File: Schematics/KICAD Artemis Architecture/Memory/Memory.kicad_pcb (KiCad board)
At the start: 4 copper layers, 100.1 x 45.8 mm, 11 parts, among them IC1 AT28C64B-15PU, IC2 AS7C164A-15PCN, IC3 AT28C64B-15PU, IC4 AS7C164A-15PCN, J1 Bus LB, J2 Bus UB, J3 Control, J4 Power, J5 Address, U1 74LS00

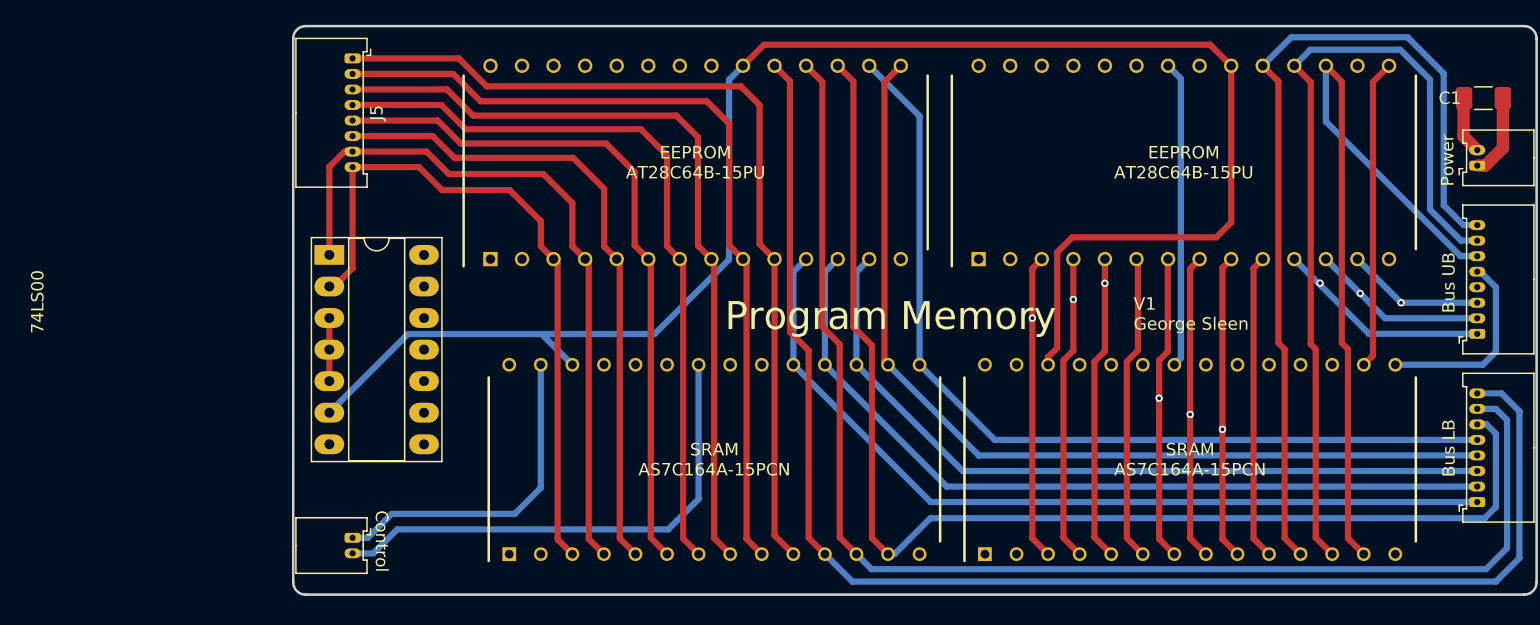
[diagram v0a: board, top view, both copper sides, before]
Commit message: Finished Program Memory PCB
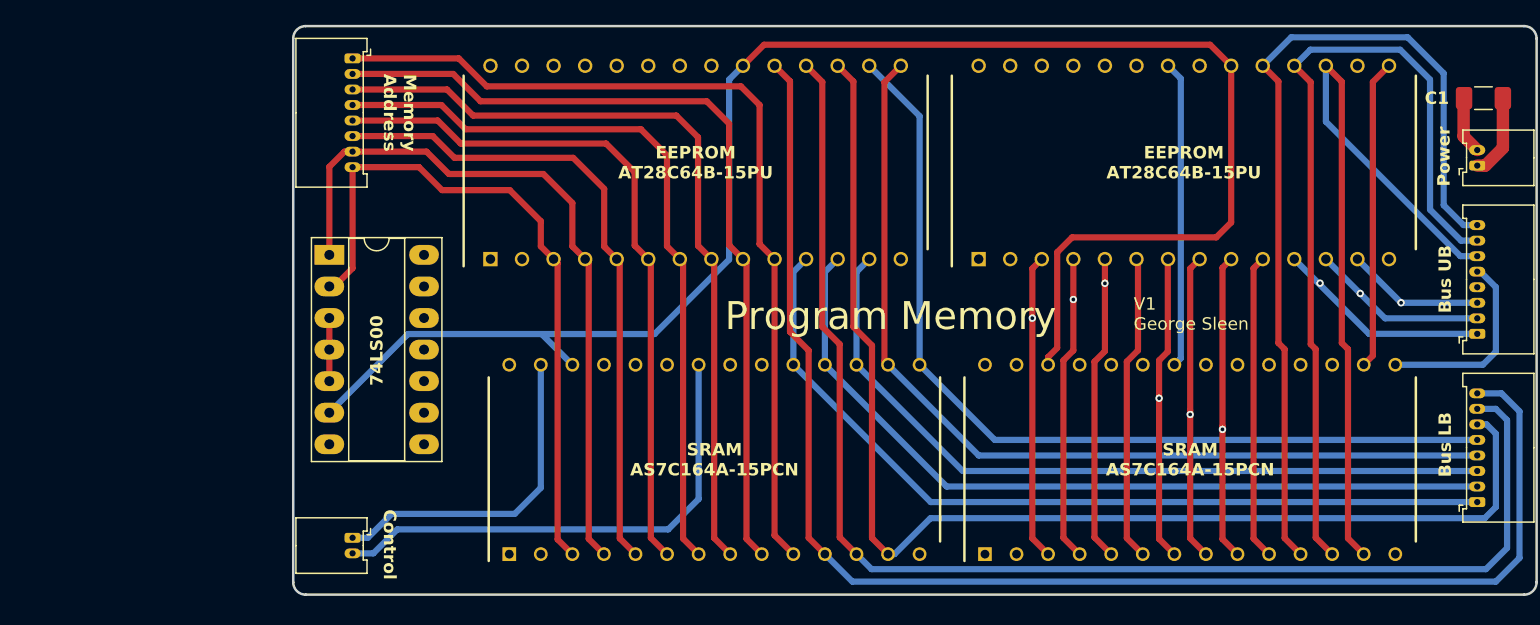
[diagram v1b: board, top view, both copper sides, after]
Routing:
- net /~{MW}: track 66.9 -> 67.9 mm
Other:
- board text added: "Memory Address"
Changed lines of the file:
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@@
 		(tags "capacitor handsolder")
 		(property "Reference" "C1"
-			(at 2.7 0 0)
+			(at 3.75 0 0)
 			(layer "F.SilkS")
 			(effects
 				(font
 					(size 1 1)
-					(thickness 0.15)
+					(thickness 0.2)
+					(bold yes)
 				)
 			)
@@
 			(at 4.38 -1.95 90)
 			(layer "F.SilkS")
+			(hide yes)
 			(effects
 				(font
@@
 	)
 	(gr_text "Bus LB"
-		(at 190.8 90.3 90)
+		(at 190.5 90.3 90)
 		(layer "F.SilkS")
 		(effects
 			(font
 				(size 1 1)
-				(thickness 0.15)
+				(thickness 0.2)
+				(bold yes)
 			)
 			(justify left bottom)
@@
 	)
 	(gr_text "Control"
-		(at 103.75 92.960714 270)
+		(at 104.4 92.885714 270)
 		(layer "F.SilkS")
 		(effects
 			(font
 				(size 1 1)
-				(thickness 0.15)
+				(thickness 0.2)
+				(bold yes)
 			)
 			(justify left bottom)
@@
 	)
 	(gr_text "74LS00"
-		(at 77.25 78.75 90)
+		(at 104.53175 82.945715 90)
 		(layer "F.SilkS")
 		(effects
 			(font
 				(size 1 1)
-				(thickness 0.15)
+				(thickness 0.2)
+				(bold yes)
 			)
 			(justify left bottom)
@@
 	)
 	(gr_text "Power"
-		(at 190.7 66.9 90)
+		(at 190.4 66.9 90)
 		(layer "F.SilkS")
 		(effects
 			(font
 				(size 1 1)
-				(thickness 0.15)
+				(thickness 0.2)
+				(bold yes)
 			)
 			(justify left bottom)
@@
 	)
 	(gr_text "Bus UB"
-		(at 190.8 77.1 90)
+		(at 190.5 77.1 90)
 		(layer "F.SilkS")
 		(effects
 			(font
 				(size 1 1)
-				(thickness 0.15)
+				(thickness 0.2)
+				(bold yes)
 			)
 			(justify left bottom)
 		)
 	)
+	(gr_text "Memory\nAddress"
+		(at 104.4 60.975 270)
+		(layer "F.SilkS")
+		(effects
+			(font
+				(size 1 1)
+				(thickness 0.2)
+				(bold yes)
+			)
+			(justify bottom)
+		)
+	)
 	(gr_text "EEPROM\nAT28C64B-15PU"
 		(at 168.89 66.377722 0)
@@
 			(font
 				(size 1 1)
-				(thickness 0.15)
+				(thickness 0.2)
+				(bold yes)
 			)
 			(justify bottom)
@@
 			(font
 				(size 1 1)
-				(thickness 0.15)
+				(thickness 0.2)
+				(bold yes)
 			)
 			(justify bottom)
@@
 			(font
 				(size 1 1)
-				(thickness 0.15)
+				(thickness 0.2)
+				(bold yes)
 			)
 			(justify bottom)
@@
 			(font
 				(size 1 1)
-				(thickness 0.15)
+				(thickness 0.2)
+				(bold yes)
 			)
 			(justify bottom)
@@
 	)
 	(segment
-		(start 118.176 72.75)
-		(end 122.926 77.5)
+		(start 122.576 77.15)
+		(end 156.35 77.15)
 		(width 0.5)
 		(layer "In2.Cu")
@@
 	)
 	(segment
-		(start 122.926 77.5)
+		(start 156.35 77.15)
 		(end 156.7 77.5)
 		(width 0.5)
@@
 	)
 	(segment
+		(start 118.176 72.75)
+		(end 122.576 77.15)
+		(width 0.5)
+		(layer "In2.Cu")
+		(net 7)
+	)
+	(segment
 		(start 119.6865 68.2365)
 		(end 119.6865 71.7205)
@@
 	)
 	(segment
-		(start 120.716 72.75)
-		(end 123.966 76)
+		(start 123.666 75.7)
+		(end 159.7 75.7)
 		(width 0.5)
 		(layer "In2.Cu")
@@
 	)
 	(segment
-		(start 123.966 76)
+		(start 159.7 75.7)
 		(end 160 76)
 		(width 0.5)
@@
 	)
 	(segment
+		(start 120.716 72.75)
+		(end 123.666 75.7)
+		(width 0.5)
+		(layer "In2.Cu")
+		(net 9)
+	)
+	(segment
 		(start 192.5 65.225)
 		(end 193.15 65.225)
@@
 	)
 	(segment
+		(start 154.05 78.65)
+		(end 119.748 78.65)
+		(width 0.5)
+		(layer "In2.Cu")
+		(net 29)
+	)
+	(segment
 		(start 155.428 81.25)
-		(end 153.178 79)
+		(end 155.428 80.028)
 		(width 0.5)
 		(layer "In2.Cu")
@@
 	)
 	(segment
-		(start 153.178 79)
-		(end 119.398 79)
+		(start 155.428 80.028)
+		(end 154.05 78.65)
 		(width 0.5)
 		(layer "In2.Cu")
@@
 	)
 	(segment
-		(start 119.398 79)
+		(start 119.748 78.65)
 		(end 117.148 81.25)
 		(width 0.5)
@@
 	(segment
 		(start 123.256 72.75)
-		(end 125.206 74.7)
+		(end 124.756 74.25)
 		(width 0.5)
 		(layer "In2.Cu")
@@
 	)
 	(segment
-		(start 125.206 74.7)
+		(start 162.09 74.25)
 		(end 162.54 74.7)
 		(width 0.5)
 		(layer "In2.Cu")
+		(net 32)
+	)
+	(segment
+		(start 124.756 74.25)
+		(end 162.09 74.25)
+		(width 0.5)
+		(layer "In2.Cu")

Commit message: Memory rework pt.1
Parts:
- removed J5: Address, Connector_Molex:Molex_PicoBlade_53048-0810_1x08_P1.25mm_Horizontal
- added C2: 0.1 uF, Capacitor_SMD:C_1206_3216Metric_Pad1.33x1.80mm_HandSolder, F.Cu at (195.5, 50.2)
- added D1: LED, LED_SMD:LED_1206_3216Metric_Pad1.42x1.75mm_HandSolder, F.Cu at (211.3, 114.9)
- added D2: LED, LED_SMD:LED_1206_3216Metric_Pad1.42x1.75mm_HandSolder, F.Cu at (211.3, 118.3)
- added D3: LED, LED_SMD:LED_1206_3216Metric_Pad1.42x1.75mm_HandSolder, F.Cu at (211.3, 121.7)
- added D4: LED, LED_SMD:LED_1206_3216Metric_Pad1.42x1.75mm_HandSolder, F.Cu at (211.3, 125.1)
- added D5: LED, LED_SMD:LED_1206_3216Metric_Pad1.42x1.75mm_HandSolder, F.Cu at (211.3, 128.5)
- added D6: LED, LED_SMD:LED_1206_3216Metric_Pad1.42x1.75mm_HandSolder, F.Cu at (211.3, 131.8)
- added D7: LED, LED_SMD:LED_1206_3216Metric_Pad1.42x1.75mm_HandSolder, F.Cu at (211.3, 135.2)
- added D8: LED, LED_SMD:LED_1206_3216Metric_Pad1.42x1.75mm_HandSolder, F.Cu at (211.3, 138.6)
- added R1: 220, Resistor_SMD:R_1206_3216Metric_Pad1.30x1.75mm_HandSolder, F.Cu at (217.2, 114.8)
- added R2: 220, Resistor_SMD:R_1206_3216Metric_Pad1.30x1.75mm_HandSolder, F.Cu at (217.2, 118.1)
- added R3: 220, Resistor_SMD:R_1206_3216Metric_Pad1.30x1.75mm_HandSolder, F.Cu at (217.2, 121.4)
- added R4: 220, Resistor_SMD:R_1206_3216Metric_Pad1.30x1.75mm_HandSolder, F.Cu at (217.2, 124.7)
- added R5: 220, Resistor_SMD:R_1206_3216Metric_Pad1.30x1.75mm_HandSolder, F.Cu at (217.2, 128.0)
- added R6: 220, Resistor_SMD:R_1206_3216Metric_Pad1.30x1.75mm_HandSolder, F.Cu at (217.2, 131.3)
- added R7: 220, Resistor_SMD:R_1206_3216Metric_Pad1.30x1.75mm_HandSolder, F.Cu at (217.2, 134.6)
- added R8: 220, Resistor_SMD:R_1206_3216Metric_Pad1.30x1.75mm_HandSolder, F.Cu at (217.2, 137.9)
- added U2: 74LS173, Package_DIP:DIP-16_W7.62mm_Socket_LongPads, F.Cu at (138.7, 102.9)
- added U4: 74LS173, Package_DIP:DIP-16_W7.62mm_Socket_LongPads, F.Cu at (162.7, 102.5)
- J3, J4: footprint Connector_Molex:Molex_PicoBlade_53048-0210_1x02_P1.25mm_Horizontal -> Connector_Molex:Molex_PicoBlade_53048-0410_1x04_P1.25mm_Horizontal
- moved U1 68.2 mm to (164.3, 49.4), turned to 90 degrees
- moved C1 13.1 mm to (195.5, 46.9), turned to 0 degrees
- moved IC2 11.5 mm to (123.7, 80.1)
- moved IC4 11.0 mm to (162.8, 80.1)
- moved J3 8.76 mm to (95.3, 89.5)
- moved IC1 7.26 mm to (123.3, 61.4)
- moved IC3 7.00 mm to (162.8, 61.6)
- moved J2 6.79 mm to (193.3, 72.0)
- moved J4 6.75 mm to (193.3, 58.5)
- moved J1 6.24 mm to (193.6, 86.2)
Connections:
- net /A0 renamed Net-(D8-A)
- net /A1 renamed Net-(D7-A)
- net /A2 renamed Net-(D6-A)
- net /A3 renamed Net-(D5-A)
- net /A4 renamed Net-(D4-A)
- net /A5 renamed Net-(D3-A)
- net /A6 renamed Net-(D2-A)
- net /A7 renamed Net-(D1-A)
- IC1 pad 22: /~{MR} -> /~{MvR}
- IC2 pad 22: /~{MR} -> /~{MvR}
- IC2 pad 27: /~{MW} -> /~{MvW}
- IC3 pad 22: /~{MR} -> /~{MvR}
- IC4 pad 22: /~{MR} -> /~{MvR}
- IC4 pad 27: /~{MW} -> /~{MvW}
- J3 pad 1: /~{MW} -> /~{MaI}
- J3 pad 2: /~{MR} -> /~{MvW}
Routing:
- net /~{MR}: track 146.0 -> 0.00 mm
- net Net-(D8-A): track 135.7 -> 0.00 mm
- net Net-(IC1-~{CE}): track 134.5 -> 0.00 mm
- net Net-(D7-A): track 133.4 -> 0.00 mm, vias 1 -> 0
- net Net-(D6-A): track 130.3 -> 0.00 mm, vias 1 -> 0
- net Net-(D5-A): track 126.9 -> 0.00 mm, vias 1 -> 0
- net Net-(D2-A): track 123.4 -> 0.00 mm, vias 1 -> 0
- net Net-(D4-A): track 121.8 -> 0.00 mm
- net Net-(D1-A): track 120.5 -> 0.00 mm, vias 1 -> 0
- net Net-(D3-A): track 117.2 -> 0.00 mm, vias 1 -> 0
- net /BUS 7: track 114.4 -> 0.00 mm
- net /BUS 6: track 107.6 -> 0.00 mm
- net /BUS 5: track 99.2 -> 0.00 mm
- net /BUS 3: track 75.2 -> 0.00 mm
- net /BUS 4: track 73.1 -> 0.00 mm
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- removed copper zone on In1.Cu, net GNDREF
- removed copper zone on In2.Cu, net VCC
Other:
- board outline removed
- board text removed: "74LS00"
- board text removed: "Bus LB"
- board text removed: "Bus UB"
- board text removed: "Control"
- board text removed: "EEPROM AT28C64B-15PU"
- board text removed: "Memory Address"
- board text removed: "Power"
- board text removed: "Program Memory"
- board text removed: "SRAM AS7C164A-15PCN"
- board text removed: "V1 George Sleen"

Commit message: Program Memory PCB
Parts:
- moved D8 51.8 mm to (196.2, 89.1), turned to 90 degrees
- moved D7 49.6 mm to (193.1, 89.1), turned to 90 degrees
- moved R8 48.1 mm to (196.3, 94.6), turned to -90 degrees
- moved D6 47.8 mm to (190.0, 89.1), turned to 90 degrees
- moved R1 47.4 mm to (174.4, 94.6), turned to -90 degrees
- moved R7 46.7 mm to (193.1, 94.6), turned to -90 degrees
- moved D5 46.3 mm to (186.9, 89.1), turned to 90 degrees
- moved R2 46.2 mm to (177.5, 94.6), turned to -90 degrees
- moved R6 45.7 mm to (190.0, 94.6), turned to -90 degrees
- moved R3 45.4 mm to (180.6, 94.6), turned to -90 degrees
- moved D4 45.3 mm to (183.8, 89.1), turned to 90 degrees
- moved R5 45.1 mm to (186.9, 94.6), turned to -90 degrees
- moved R4 45.0 mm to (183.8, 94.6), turned to -90 degrees
- moved D 45.0 mm to (174.4, 89.1), turned to 90 degrees
- moved D3 44.8 mm to (180.7, 89.1), turned to 90 degrees
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- renumbered D1 to D
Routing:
- net Net-(IC1-~{CE}): track 0.00 -> 177.2 mm, vias 0 -> 2
- net VCC: track 0.00 -> 175.9 mm, vias 0 -> 2
- net Net-(D2-A): track 0.00 -> 161.1 mm, vias 0 -> 4
- net Net-(D1-A): track 0.00 -> 149.7 mm, vias 0 -> 1
- net Net-(D5-A): track 0.00 -> 136.4 mm
- net Net-(D8-A): track 0.00 -> 135.3 mm
- net Net-(D7-A): track 0.00 -> 134.7 mm
- net Net-(D6-A): track 0.00 -> 133.3 mm
- net Net-(D4-A): track 0.00 -> 130.6 mm
- net Net-(D3-A): track 0.00 -> 130.5 mm
- net /~{MvR}: track 0.00 -> 124.4 mm
- net /BUS 7: track 0.00 -> 114.5 mm
- net /BUS 2: track 0.00 -> 112.9 mm
- net /BUS 1: track 0.00 -> 112.8 mm
- net /BUS 0: track 0.00 -> 112.8 mm
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- added copper zone on In1.Cu, net GNDREF
- added copper zone on In2.Cu, net VCC
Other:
- board outline added: 98.8 x 50.1 mm
- board text added: "74LS00"
- board text added: "74LS173"
- board text added: "D"
- board text added: "EEPROM-LB AT28C64B-15PU"
- board text added: "EEPROM-UB AT28C64B-15PU"
- board text added: "George Sleen"
- board text added: "Program Memory"
- board text added: "R"
- board text added: "SRAM-LB AS7C164A-15PCN"
- board text added: "SRAM-UB AS7C164A-15PCN"
- board text added: "V1"

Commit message: Finalized Program Memory PCB
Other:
- board text added: "Bus LB"
- board text added: "Bus UB"
- board text added: "Control"
- board text added: "Current Memory Address"
- board text added: "Power"
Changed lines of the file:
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@@
+		)
+	)
+	(gr_text "Bus UB"
+		(at 191.55 63.858 90)
+		(layer "F.SilkS")
+		(effects
+			(font
+				(size 1 1)
+				(thickness 0.2)
+				(bold yes)
+			)
 		)
 	)
@@
 		)
 	)
+	(gr_text "Control"
+		(at 107.25 94.4 270)
+		(layer "F.SilkS")
+		(effects
+			(font
+				(size 1 1)
+				(thickness 0.2)
+				(bold yes)
+			)
+		)
+	)
 	(gr_text "D"
 		(at 180.7 89.05 90)
@@
 		)
 	)
+	(gr_text "Power"
+		(at 191.55 53.108 90)
+		(layer "F.SilkS")
+		(effects
+			(font
+				(size 1 1)
+				(thickness 0.2)
+				(bold yes)
+			)
+		)
+	)
 	(gr_text "V1"
 		(at 122.45 95.85 0)
@@
 		)
 	)
+	(gr_text "Current Memory Address"
+		(at 188.3 85.35 0)
+		(layer "F.SilkS")
+		(effects
+			(font
+				(size 1 1)
+				(thickness 0.2)
+				(bold yes)
+			)
+		)
+	)
 	(gr_text "R"
 		(at 177.55 94.6 90)
@@
 		(layer "F.SilkS")
 		(effects
+			(font
+				(size 1 1)
+				(thickness 0.2)
+				(bold yes)
+			)
+		)
+	)
+	(gr_text "Bus LB"
+		(at 191.55 77.108001 90)
+		(layer "F.SilkS")
+		(effects
